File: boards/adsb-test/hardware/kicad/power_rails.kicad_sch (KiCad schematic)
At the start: 0 parts

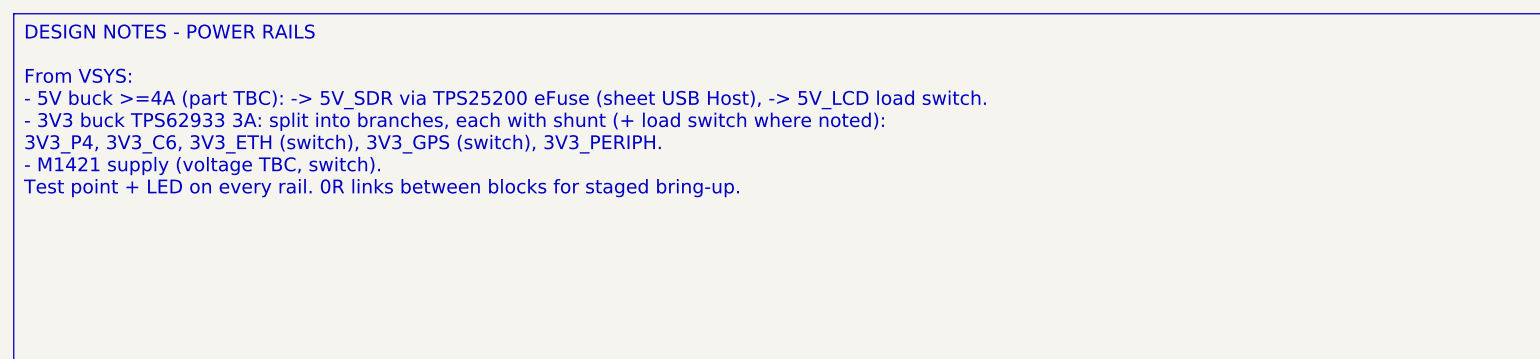
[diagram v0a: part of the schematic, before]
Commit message: Release v0.4.0: ADSB_Test with ESP32-C5, ADSBee m1421 and LA5016 header
- C6 -> C5 co-processor; m1421 identified and integrated (symbol/footprint
  from the ADSBee 1421 carrier, GPL-3.0 attribution)
- Power budget and 2S1P battery sizing for >= 1 h; USB-A for 1-2 SDRs via hub
- Dev port: FT2232H + RP2040 debugprobe; TCA6408A expander for slow I/O
- Test Debug sheet with LA5016 header and rail test points
- Vendor documents git-ignored (public repo)

Co-Authored-By: Claude Opus 5.5 <noreply@anthropic.com>
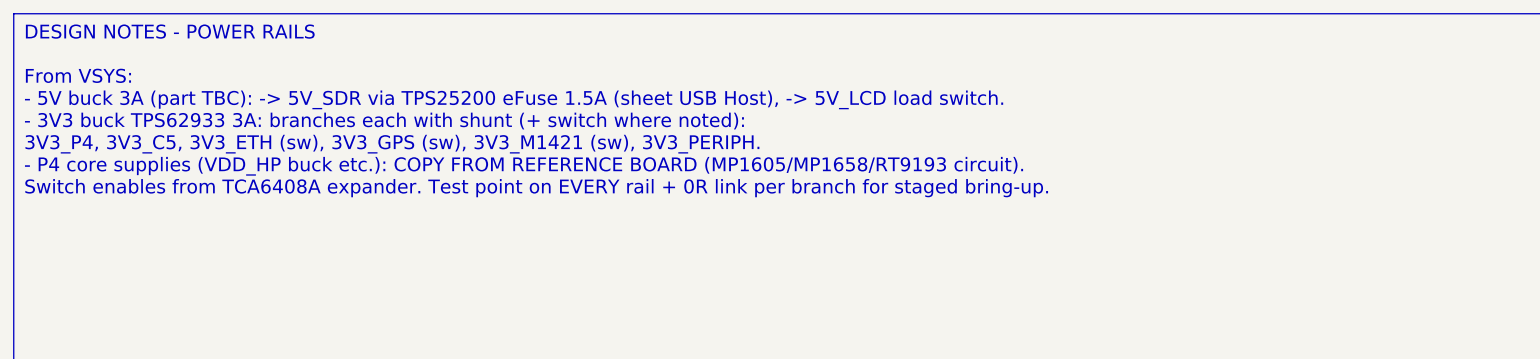
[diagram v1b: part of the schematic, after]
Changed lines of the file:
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@@
 		(comment 1 "Requirements: boards/adsb-test/docs/requirements.md")
 	)
-	(text_box "DESIGN NOTES - POWER RAILS\n\nFrom VSYS:\n- 5V buck >=4A (part TBC): -> 5V_SDR via TPS25200 eFuse (sheet USB Host), -> 5V_LCD load switch.\n- 3V3 buck TPS62933 3A: split into branches, each with shunt (+ load switch where noted):\n  3V3_P4, 3V3_C6, 3V3_ETH (switch), 3V3_GPS (switch), 3V3_PERIPH.\n- M1421 supply (voltage TBC, switch).\nTest point + LED on every rail. 0R links between blocks for staged bring-up."
+	(text_box "DESIGN NOTES - POWER RAILS\n\nFrom VSYS:\n- 5V buck 3A (part TBC): -> 5V_SDR via TPS25200 eFuse 1.5A (sheet USB Host), -> 5V_LCD load switch.\n- 3V3 buck TPS62933 3A: branches each with shunt (+ switch where noted):\n  3V3_P4, 3V3_C5, 3V3_ETH (sw), 3V3_GPS (sw), 3V3_M1421 (sw), 3V3_PERIPH.\n- P4 core supplies (VDD_HP buck etc.): COPY FROM REFERENCE BOARD (MP1605/MP1658/RT9193 circuit).\nSwitch enables from TCA6408A expander. Test point on EVERY rail + 0R link per branch for staged bring-up."
 		(exclude_from_sim no)
 		(at 20 20 0)

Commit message: Release v0.17.0: ADSB_Test power schematics (PD input, 2S charger, rails, monitors)
Co-Authored-By: Claude Opus 5.5 <noreply@anthropic.com>
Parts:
- added C411, C412, C421, C422: 10uF 25V, Capacitor_SMD:C_0805_2012Metric, symbol Device:C
- added C413, C415, C423, C425: 100nF, Capacitor_SMD:C_0402_1005Metric, symbol Device:C
- added C414, C424: 33nF, Capacitor_SMD:C_0402_1005Metric, symbol Device:C
- added C416, C417, C426, C427: 22uF 10V, Capacitor_SMD:C_1206_3216Metric, symbol Device:C
- added C430, C431, C432, C433: 1nF, Capacitor_SMD:C_0402_1005Metric, symbol Device:C
- added L411, L421: 4.7uH, Inductor_SMD:L_Bourns_SRP5030T, symbol Device:L
- added R411, R421: 100k, Resistor_SMD:R_0402_1005Metric, symbol Device:R
- added R412, R422: 28k, Resistor_SMD:R_0402_1005Metric, symbol Device:R
- added R413: 52.3k 1%, Resistor_SMD:R_0402_1005Metric, symbol Device:R
- added R414, R424: 10k 1%, Resistor_SMD:R_0402_1005Metric, symbol Device:R
- added R423: 31.6k 1%, Resistor_SMD:R_0402_1005Metric, symbol Device:R
- added R430, R431, R432, R433: 100R, Resistor_SMD:R_0402_1005Metric, symbol Device:R
- added RS401: 10m, Resistor_SMD:R_1206_3216Metric, symbol Device:R_Shunt
- added RS402: 20m, Resistor_SMD:R_1206_3216Metric, symbol Device:R_Shunt
- added RS403, RS404: 50m, Resistor_SMD:R_1206_3216Metric, symbol Device:R_Shunt
- added RS405, RS406, RS409: 100m, Resistor_SMD:R_1206_3216Metric, symbol Device:R_Shunt
- added RS407, RS408: 1R, Resistor_SMD:R_1206_3216Metric, symbol Device:R_Shunt
- added TP401: 5V, TestPoint:TestPoint_Pad_D1.0mm, symbol Connector:TestPoint
- added TP402: 3V3, TestPoint:TestPoint_Pad_D1.0mm, symbol Connector:TestPoint
- added TP403: VSYS, TestPoint:TestPoint_Pad_D1.0mm, symbol Connector:TestPoint
- added TP410: 5V_SDR, TestPoint:TestPoint_Pad_D1.0mm, symbol Connector:TestPoint
- added TP411: 5V_LCD, TestPoint:TestPoint_Pad_D1.0mm, symbol Connector:TestPoint
- added TP412: 3V3_P4, TestPoint:TestPoint_Pad_D1.0mm, symbol Connector:TestPoint
- added TP413: 3V3_C5, TestPoint:TestPoint_Pad_D1.0mm, symbol Connector:TestPoint
- added TP414: 3V3_ETH, TestPoint:TestPoint_Pad_D1.0mm, symbol Connector:TestPoint
- added TP415: 3V3_GPS, TestPoint:TestPoint_Pad_D1.0mm, symbol Connector:TestPoint
- added TP416: 3V3_M1421, TestPoint:TestPoint_Pad_D1.0mm, symbol Connector:TestPoint
- added TP417: 3V3_PERIPH, TestPoint:TestPoint_Pad_D1.0mm, symbol Connector:TestPoint
- added U411, U421: TPS62933, Package_TO_SOT_SMD:SOT-583-8, symbol Regulator_Switching:TPS62933
- added U430, U431, U432, U433: TPS22917, Package_TO_SOT_SMD:SOT-23-6, symbol Power_Management:TPS22917DBV
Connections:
- new net 3V3: RS401.4, RS404.1, RS405.1, RS406.1, RS407.1, RS408.1, RS409.1, TP402.1
- new net 3V3_BUCK: C426.1, C427.1, L421.2, R423.1, RS401.1
- new net 3V3_C5: RS405.4, TP413.1
- new net 3V3_ETH: R431.2, TP414.1, U431.6 (VOUT)
- new net 3V3_ETH_SH: RS406.4, U431.1 (VIN)
- new net 3V3_GPS: R432.2, TP415.1, U432.6 (VOUT)
- new net 3V3_GPS_SH: RS407.4, U432.1 (VIN)
- new net 3V3_M1421: R433.2, TP416.1, U433.6 (VOUT)
- new net 3V3_M1421_SH: RS408.4, U433.1 (VIN)
- new net 3V3_P4: RS404.4, TP412.1
- new net 3V3_PERIPH: RS409.4, TP417.1
- new net 5V: C416.1, C417.1, L411.2, R413.1, RS402.1, RS403.1, TP401.1
- new net 5V_LCD: R430.2, TP411.1, U430.6 (VOUT)
- new net 5V_LCD_SH: RS403.4, U430.1 (VIN)
- new net 5V_SDR: RS402.4, TP410.1
- new net B3V3_BST: C425.1, U421.6 (BST)
- new net B3V3_EN: R421.2, R422.1, U421.2 (EN)
- new net B3V3_FB: R423.2, R424.1, U421.8 (FB)
- new net B3V3_SS: C424.1, U421.7 (SS)
- new net B3V3_SW: C425.2, L421.1, U421.5 (SW)
- new net B5V_BST: C415.1, U411.6 (BST)
- new net B5V_EN: R411.2, R412.1, U411.2 (EN)
- new net B5V_FB: R413.2, R414.1, U411.8 (FB)
- new net B5V_SS: C414.1, U411.7 (SS)
- new net B5V_SW: C415.2, L411.1, U411.5 (SW)
- new net CT30: C430.1, U430.4 (CT)
- new net CT31: C431.1, U431.4 (CT)
- new net CT32: C432.1, U432.4 (CT)
- new net CT33: C433.1, U433.4 (CT)
- new net EXP_EN_ETH: U431.3 (ON)
- new net EXP_EN_GPS: U432.3 (ON)
- new net EXP_EN_LCD: U430.3 (ON)
- new net EXP_EN_M1421: U433.3 (ON)
- new net GND: C411.2, C412.2, C413.2, C414.2, C416.2, C417.2, C421.2, C422.2, C423.2, C424.2, C426.2, C427.2, C430.2, C431.2, C432.2, C433.2, R412.2, R414.2, R422.2, R424.2, U411.4 (GND), U421.4 (GND), U430.2 (GND), U431.2 (GND), U432.2 (GND), U433.2 (GND)
- new net PM1_CH4_N: RS402.3
- new net PM1_CH4_P: RS402.2
- new net PM2_CH1_N: RS403.3
- new net PM2_CH1_P: RS403.2
- new net PM2_CH2_N: RS404.3
- new net PM2_CH2_P: RS404.2
- new net PM2_CH3_N: RS405.3
- new net PM2_CH3_P: RS405.2
- new net PM2_CH4_N: RS406.3
- new net PM2_CH4_P: RS406.2
- new net PM3_CH1_N: RS407.3
- new net PM3_CH1_P: RS407.2
- new net PM3_CH2_N: RS408.3
- new net PM3_CH2_P: RS408.2
- new net PM3_CH3_N: RS409.3
- new net PM3_CH3_P: RS409.2
- new net PM3_CH4_N: RS401.3
- new net PM3_CH4_P: RS401.2
- new net QD30: R430.1, U430.5 (QOD)
- new net QD31: R431.1, U431.5 (QOD)
- new net QD32: R432.1, U432.5 (QOD)
- new net QD33: R433.1, U433.5 (QOD)
- new net VSYS: C411.1, C412.1, C413.1, C421.1, C422.1, C423.1, R411.1, R421.1, TP403.1, U411.3 (VIN), U421.3 (VIN)
- no-connect marks 0 -> 2

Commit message: Release v0.18.0: power switch, always-on VBACKUP, hand-solder footprints, PCBWay notes
Co-Authored-By: Claude Opus 5.5 <noreply@anthropic.com>
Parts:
- removed R421: 100k, Resistor_SMD:R_0402_1005Metric, symbol Device:R
- removed R422: 28k, Resistor_SMD:R_0402_1005Metric, symbol Device:R
- added SW401: POWER (slide), Button_Switch_THT:SW_Slide_SPDT_Angled_CK_OS102011MA1Q, symbol Switch:SW_SPDT
- C411, C412, C421, C422: footprint Capacitor_SMD:C_0805_2012Metric -> Capacitor_SMD:C_0805_2012Metric_Pad1.18x1.45mm_HandSolder
- C413, C414, C415, C423, C424, C425, C430, C431, C432, C433: footprint Capacitor_SMD:C_0402_1005Metric -> Capacitor_SMD:C_0805_2012Metric_Pad1.18x1.45mm_HandSolder
- C416, C417, C426, C427: footprint Capacitor_SMD:C_1206_3216Metric -> Capacitor_SMD:C_1206_3216Metric_Pad1.33x1.80mm_HandSolder
- R411, R412, R413, R414, R423, R424, R430, R431, R432, R433: footprint Resistor_SMD:R_0402_1005Metric -> Resistor_SMD:R_0805_2012Metric_Pad1.20x1.40mm_HandSolder
- RS401, RS402, RS403, RS404, RS405, RS406, RS407, RS408, RS409: footprint Resistor_SMD:R_1206_3216Metric -> Resistor_SMD:R_1206_3216Metric_Pad1.30x1.75mm_HandSolder
- TP401, TP402, TP403, TP410, TP411, TP412, TP413, TP414, TP415, TP416, TP417: footprint TestPoint:TestPoint_Pad_D1.0mm -> TestPoint:TestPoint_Pad_D1.5mm
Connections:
- net B5V_EN is gone; now on net PWR_EN: R411.2, R412.1, U411.2 (EN)
- net GND: now also SW401.3 (C)
- net B3V3_EN renamed PWR_EN
- net PWR_EN: now also SW401.2 (B)
- no-connect marks 2 -> 3
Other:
- note added: "POWER: SW401 OFF = PWR_EN low = both bucks off. VSYS, charger and VBACKUP stay alive."

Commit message: Release v0.19.0: hand-solder footprints (m1421, QFNs, SOT-23, SO-8), Rev 1 hand assembly
Co-Authored-By: Claude Opus 5.5 <noreply@anthropic.com>
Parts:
- U411, U421: footprint Package_TO_SOT_SMD:SOT-583-8 -> ADSB_Test:SOT-583-8_HandSolder
- U430, U431, U432, U433: footprint Package_TO_SOT_SMD:SOT-23-6 -> Package_TO_SOT_SMD:SOT-23-6_Handsoldering

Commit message: Release v0.21.0: WT01P4C5-S1 module (P4+C5) and DS3231M RTC for ADSB_Test
Co-Authored-By: Claude Opus 5.5 <noreply@anthropic.com>
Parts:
- RS404: value 50m -> 20m
- TP412: value 3V3_P4 -> 5V_MCU
- TP413: value 3V3_C5 -> 3V3_SD
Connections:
- net 3V3: no longer RS404.1
- net 5V: now also RS404.1
- net 3V3_C5 renamed 3V3_SD
- net 3V3_P4 renamed 5V_MCU

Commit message: Release v0.24.0: OSPTEK ESP32-P4C5 Core module replaces WT01P4C5-S1
Co-Authored-By: Claude Opus 5.5 <noreply@anthropic.com>
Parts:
- RS404: value 20m -> 50m
- TP412: value 5V_MCU -> 3V3_MCU
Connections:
- net 3V3: now also RS404.1
- net 5V: no longer RS404.1
- net 5V_MCU renamed 3V3_MCU

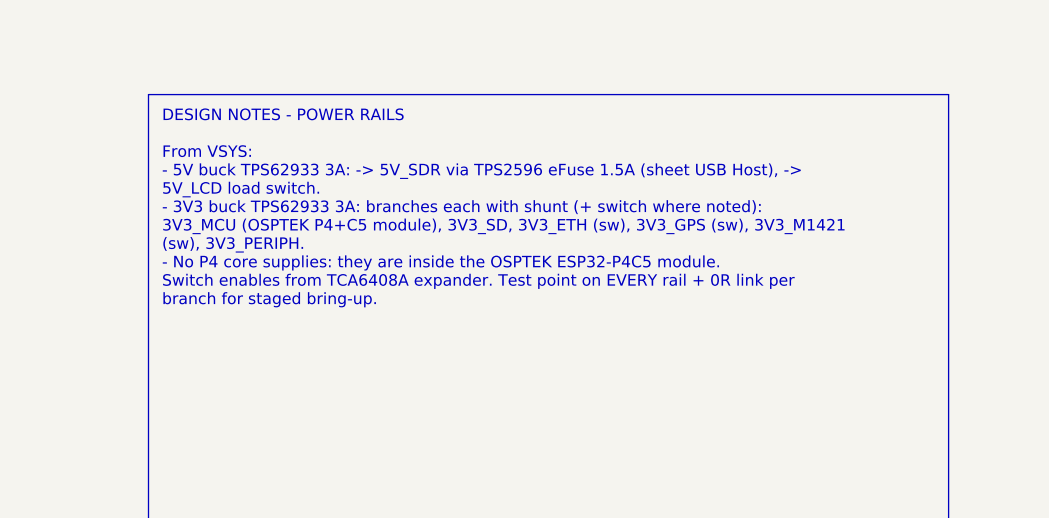
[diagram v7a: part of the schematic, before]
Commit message: Schematic generator: hide stacked pins (KiCad convention) so pin numbers don't overprint
Co-Authored-By: Claude Opus 5.5 <noreply@anthropic.com>
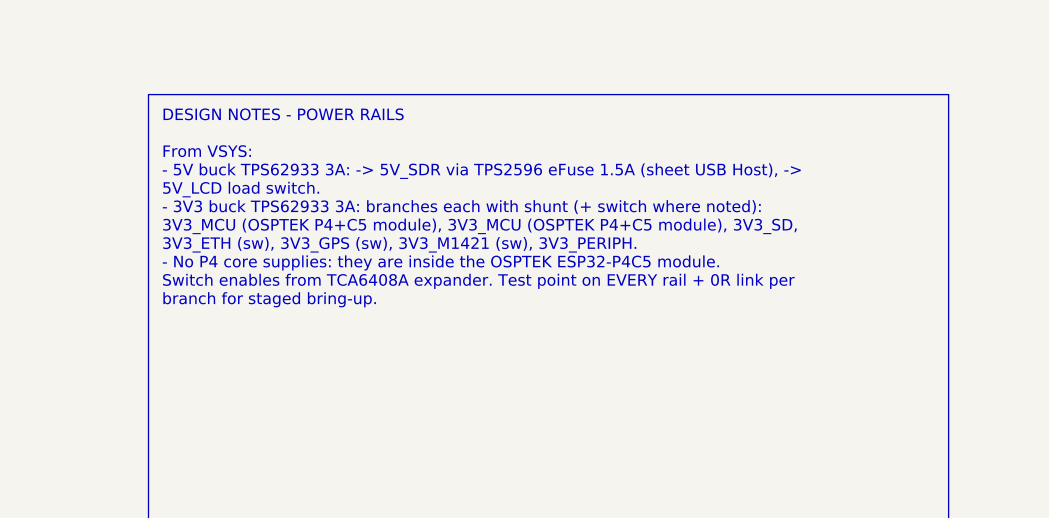
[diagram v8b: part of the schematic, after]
